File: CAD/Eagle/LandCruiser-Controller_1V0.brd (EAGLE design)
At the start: 99 x 64.8 mm, 58 parts, among them K311 V23086C1001A403, K312 V23086C1001A403, K313 V23086C1001A403, K314 V23086C1001A403, K315 V23086C1001A403, U101 MEGA8-P, U221 SN75240, U301 MIC2981/2982SO18W, U501 MAX232_SOIC16, U611 LM7805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

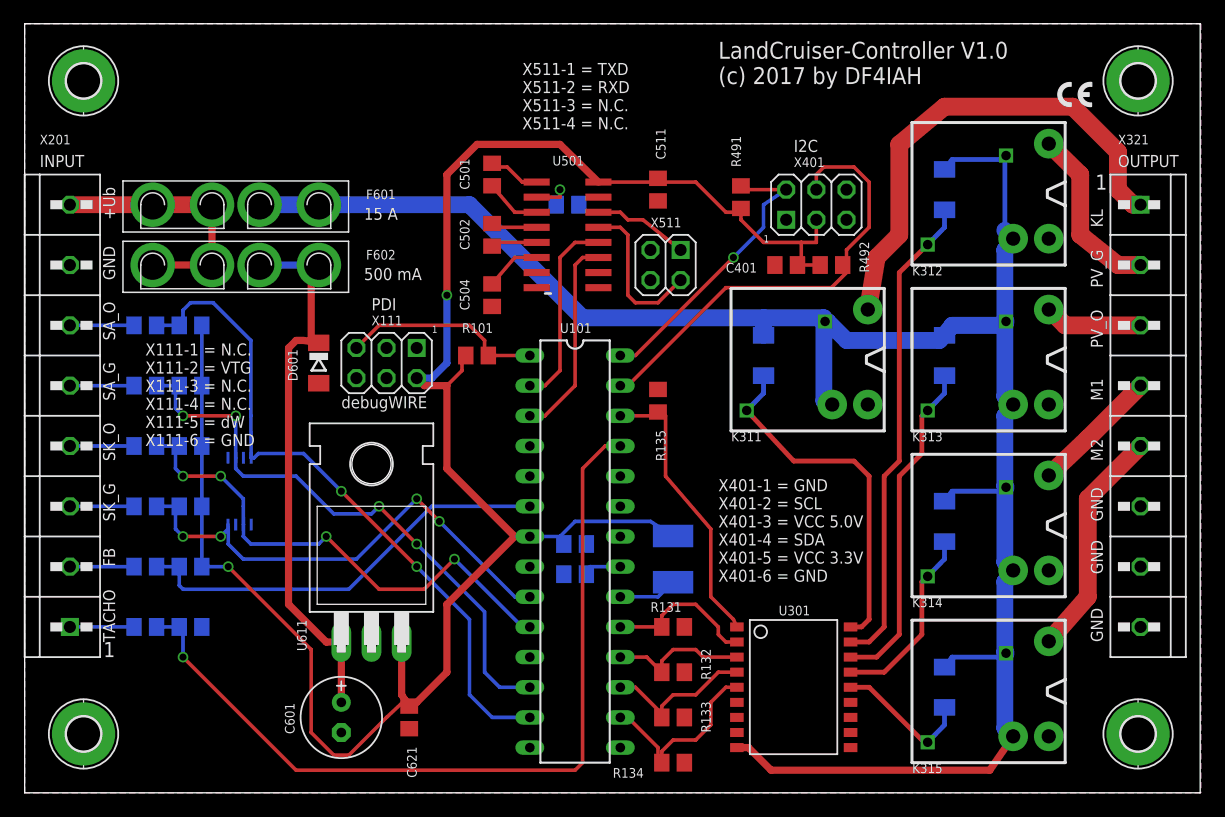
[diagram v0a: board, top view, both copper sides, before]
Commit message: HW_V1.0 - Routing - GND vias added, place below the LM7805 cleared
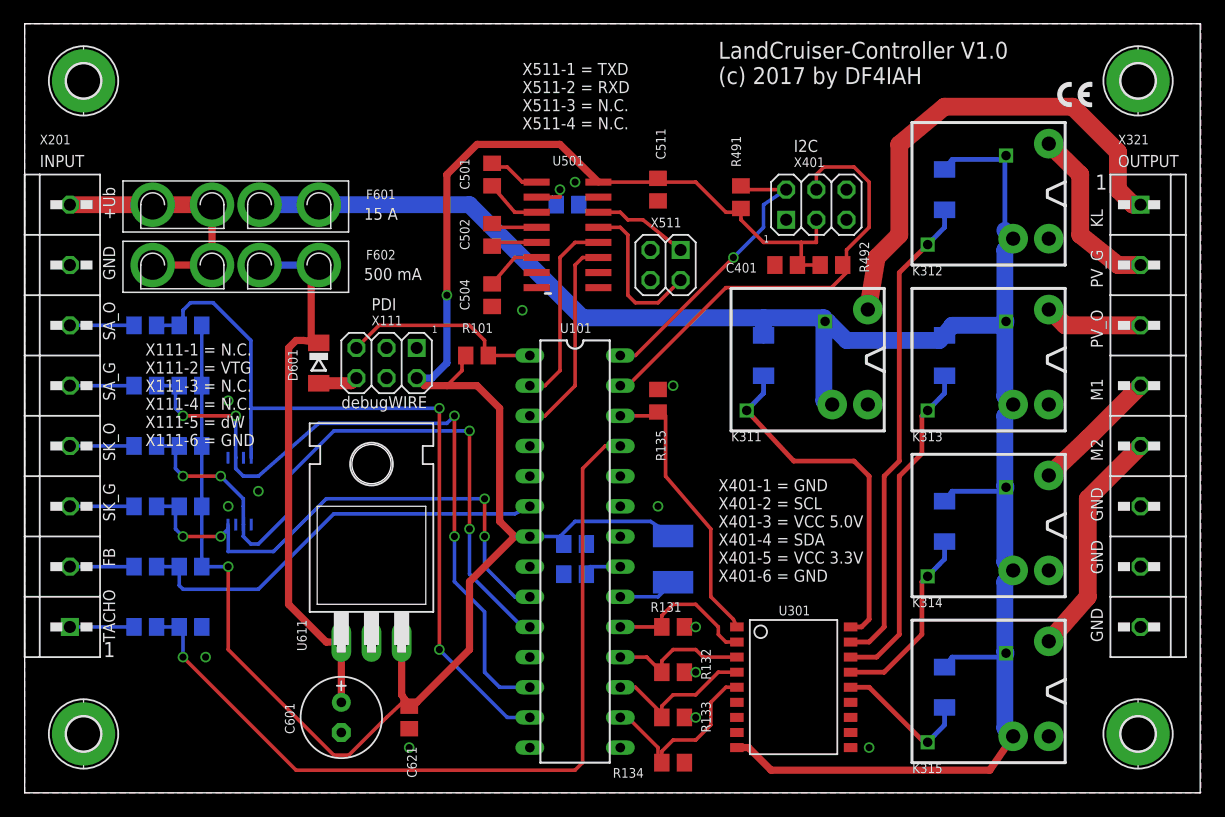
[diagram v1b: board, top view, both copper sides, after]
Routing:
- net MP_SK_O: track 43.8 -> 57.9 mm
- net MP_SA_G: track 49.6 -> 61.3 mm
- net MP_SA_O: track 57.0 -> 66.6 mm
- net GND: track 0.00 -> 3.35 mm, vias 0 -> 13
- net MP_SK_G: track 41.9 -> 45.1 mm
- net +5V: track 171.3 -> 172.8 mm

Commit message: HW_V1.0 - additional capacitors added
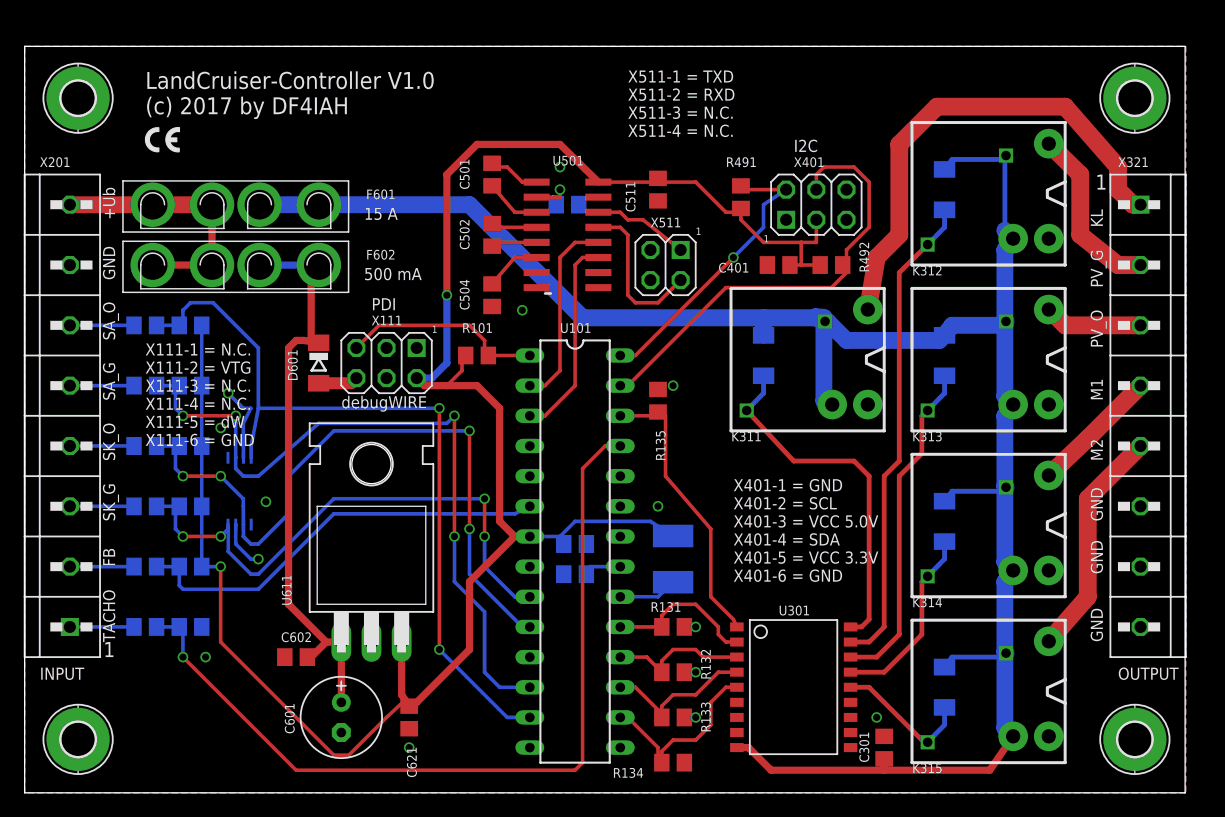
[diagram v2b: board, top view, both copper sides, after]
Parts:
- added C301, C602: 100nF, rcl:C0805
- moved H701 1.53 mm to (4.50, 58.5)
- moved H702 1.48 mm to (93.5, 58.5)
- moved H703 0.65 mm to (4.50, 4.50)
- moved C401 0.64 mm to (63.5, 44.5)
- moved H704 0.53 mm to (93.5, 4.50)
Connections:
- net +12V: now also C301.1
- net GND: now also C301.2, C602.2
- net REGIN: now also C602.1
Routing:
- net GND: track 3.35 -> 14.2 mm, vias 13 -> 14
- net REGIN: track 47.4 -> 49.5 mm
- net +12V: track 170.4 -> 172.1 mm
- net MP_SK_G: track 45.1 -> 46.7 mm
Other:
- board size 99 x 64.8 mm -> 97.7 x 62.9 mm
- board text added: "4x 2.8 mm"

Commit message: HW_V1.0 - status LED added, ADC0 connected to 15:1 divider for 12V control
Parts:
- added C631: 1nF, rcl:C0805
- added D141: red, df4iah_diode:LED_2PIN-TTH
- added R141: 330R, rcl:R0805
- added R631: 18kR, rcl:R0805
- added R632: 247kR, rcl:R0805
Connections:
- new net LED_A: D141.A, R141.2
- new net MP_ADC0: C631.1, R631.2, R632.1, U101.23
- new net MP_ADC1: U101.24
- new net MP_LED: R141.1, U101.5
- net +12V: now also R632.2
- net GND: now also C631.2, D141.C, R631.1
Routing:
- net MP_ADC0: track 0.00 -> 40.6 mm
- net GND: track 14.2 -> 28.7 mm
- net LED_A: track 0.00 -> 13.1 mm
- net MP_LED: track 0.00 -> 3.49 mm
- net +12V: track 172.1 -> 175.0 mm
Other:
- board size 97.7 x 62.9 mm -> 98 x 62.9 mm
- board text added: "+12V"
- board text removed: "+Ub"

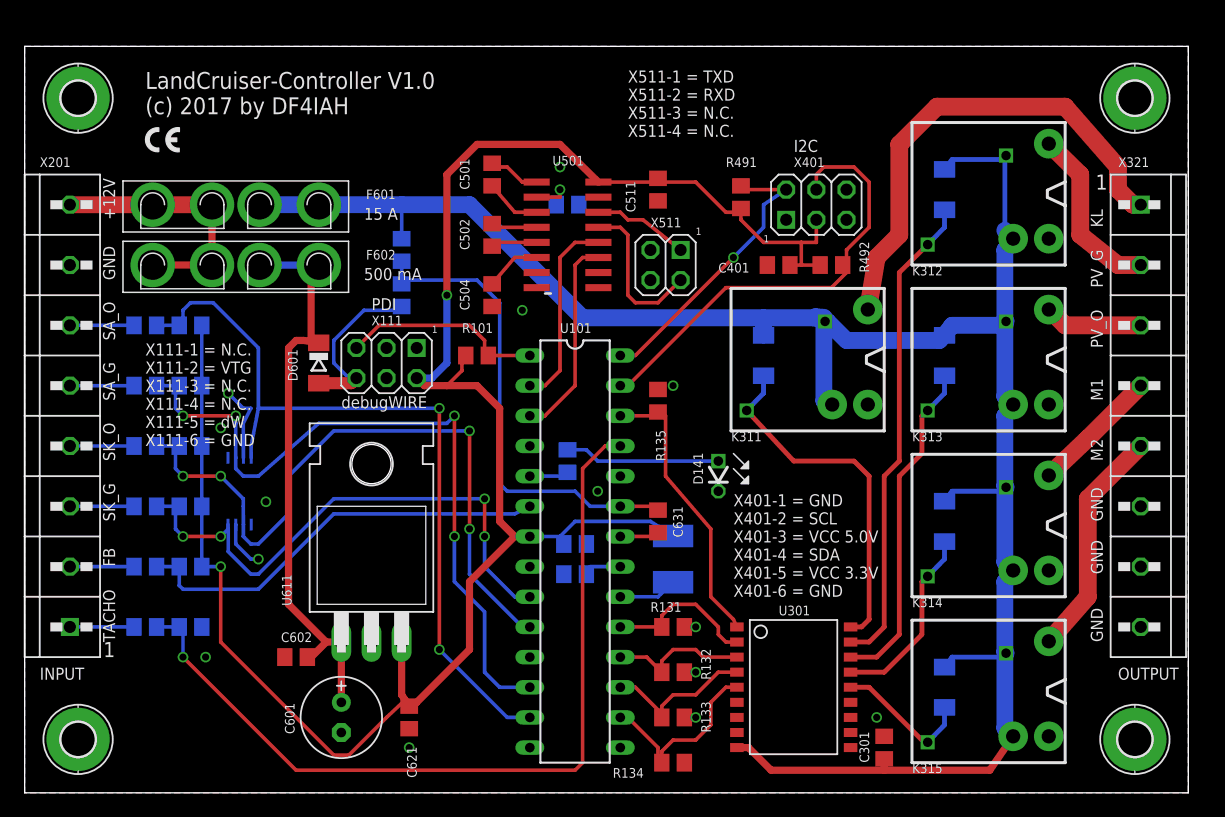
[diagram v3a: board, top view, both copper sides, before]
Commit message: HW_V1.0 - dimension values rounded, pad below the LM7805 restricted
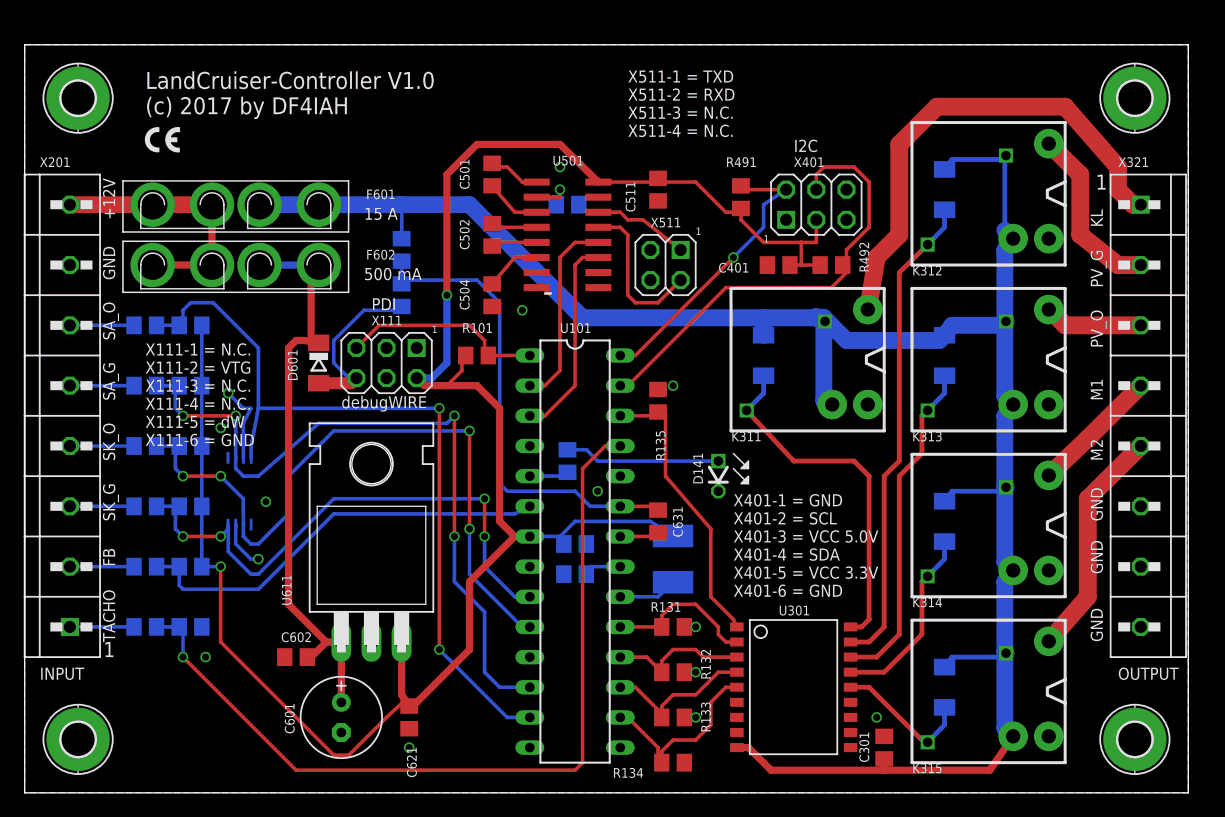
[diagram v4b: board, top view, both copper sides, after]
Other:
- board size 98 x 62.9 mm -> 98 x 63 mm
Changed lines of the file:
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@@
 <plain>
 <wire x1="0" y1="0" x2="98" y2="0" width="0" layer="20"/>
-<wire x1="98" y1="0" x2="98" y2="62.865" width="0" layer="20"/>
-<wire x1="98" y1="62.865" x2="0" y2="62.865" width="0" layer="20"/>
-<wire x1="0" y1="62.865" x2="0" y2="0" width="0" layer="20"/>
-<dimension x1="0" y1="0" x2="0" y2="62.865" x3="-8.5" y3="31.4325" textsize="1.016" layer="47"/>
+<wire x1="98" y1="0" x2="98" y2="63" width="0" layer="20"/>
+<wire x1="98" y1="63" x2="0" y2="63" width="0" layer="20"/>
+<wire x1="0" y1="63" x2="0" y2="0" width="0" layer="20"/>
+<dimension x1="0" y1="0" x2="0" y2="63" x3="-8.5" y3="31.5" textsize="1.016" layer="47"/>
 <dimension x1="0" y1="62.865" x2="98" y2="62.865" x3="49" y3="70.935" textsize="1.016" layer="47"/>
 <text x="10.16" y="57.15" size="1.4224" layer="21" ratio="15">LandCruiser-Controller V1.0
@@
 <dimension x1="93.5" y1="58.5" x2="0" y2="58.5" x3="46.75" y3="67.96978125" textsize="0.8128" layer="47"/>
 <text x="7.62" y="1.27" size="0.8128" layer="51">4x 2.8 mm</text>
+<polygon width="0.3048" layer="41">
+<vertex x="23.495" y="31.75"/>
+<vertex x="34.925" y="31.75"/>
+<vertex x="34.925" y="14.605"/>
+<vertex x="23.495" y="14.605"/>
+</polygon>
 </plain>
 <attributes>
@@
 <polygon width="0.3" layer="16">
 <vertex x="0" y="0"/>
-<vertex x="0" y="62.865"/>
-<vertex x="98" y="62.865"/>
+<vertex x="0" y="63"/>
+<vertex x="98" y="63"/>
 <vertex x="98" y="0"/>
 </polygon>
 <polygon width="0.3" layer="1">
 <vertex x="0" y="0"/>
-<vertex x="0" y="62.865"/>
-<vertex x="98" y="62.865"/>
+<vertex x="0" y="63"/>
+<vertex x="98" y="63"/>
 <vertex x="98" y="0"/>
 </polygon>

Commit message: HW_V1.0 - fuse drillings added - V1.0 finished and ordered
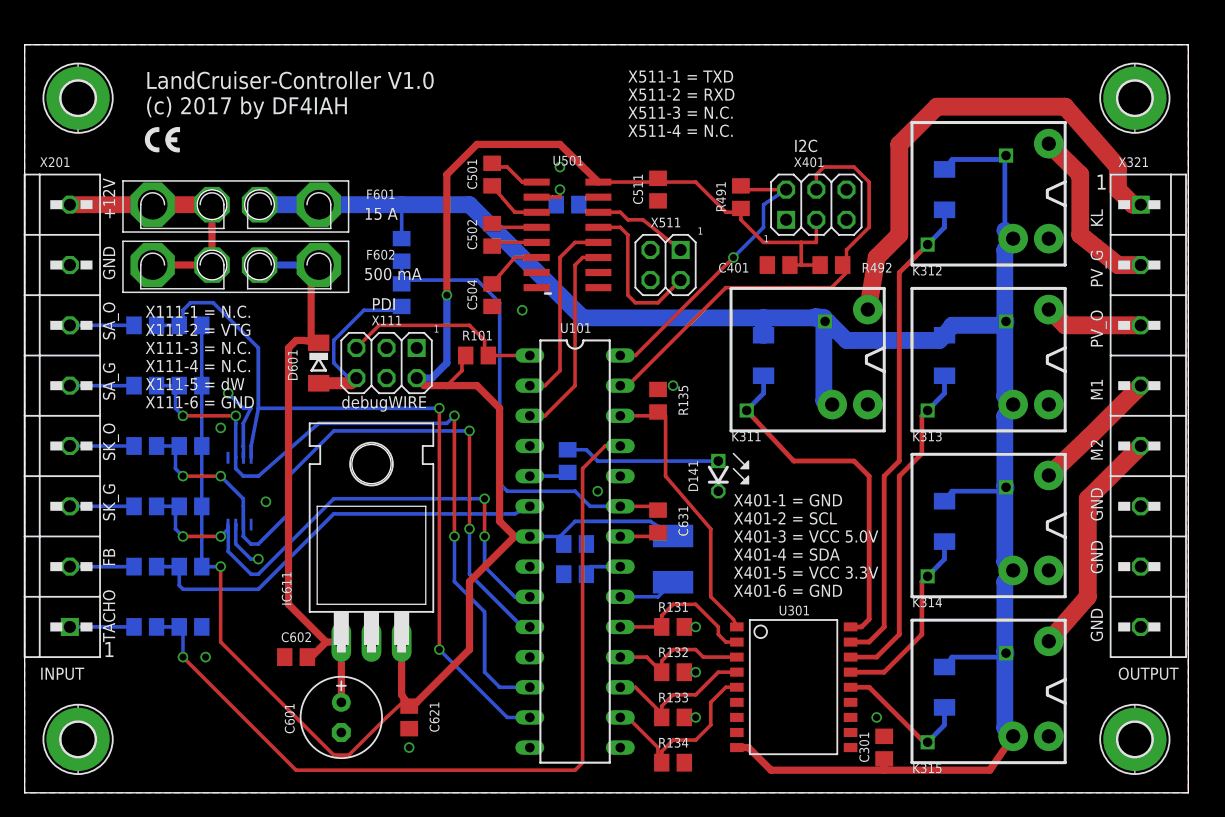
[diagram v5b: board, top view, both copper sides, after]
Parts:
- renumbered U611 to IC611
